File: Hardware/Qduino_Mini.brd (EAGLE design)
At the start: 20.3 x 38.1 mm, 41 parts, among them J1 LiPo, Q1 PFET, U1 ATMEGA32U41:1-LESS_PASTE, U2 MCP73831, U3 MAX17048, U4 AP2112K-3.3TRG-1, U5 MIGHTYQ-L-SILK, Y1 8MHZ

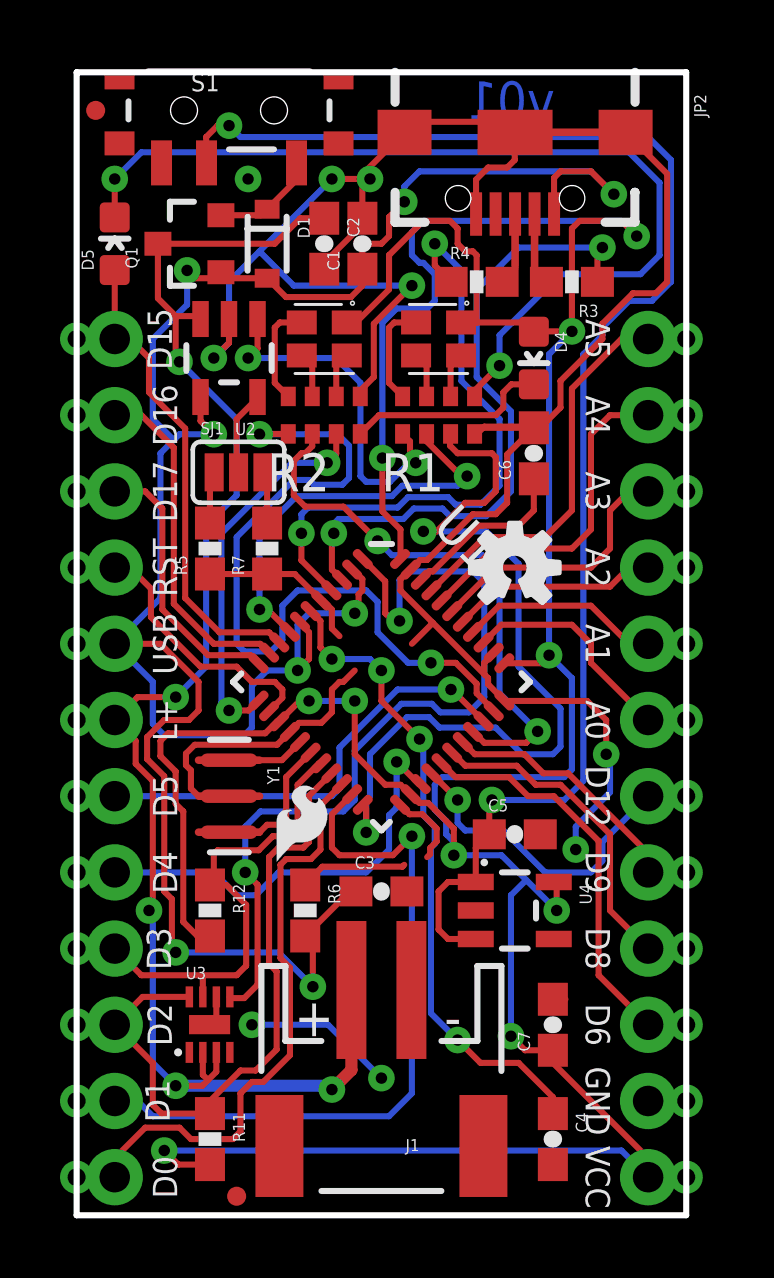
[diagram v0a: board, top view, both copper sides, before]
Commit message: Labled LED flags to the colors ther were hooked up to and replaced the RGB LEDs with the footprint for the new part.  STUFF IS BROKEN.
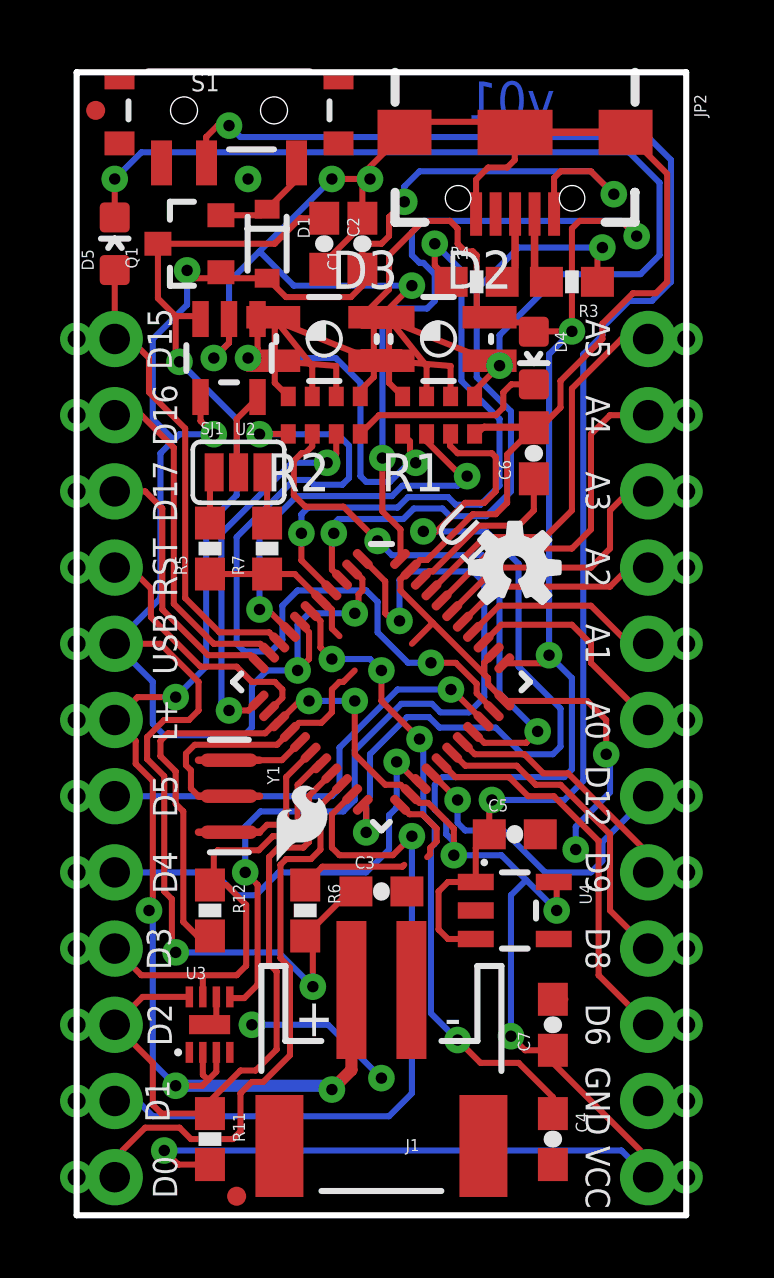
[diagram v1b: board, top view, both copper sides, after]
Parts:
- D2, D3: device Spark:PLCC4-2MM-RGB -> Testing:P-LCC-4-3
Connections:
- net N$1: now also D2.3; no longer D2.RED
- net N$2: now also D2.2; no longer D2.BLUE
- net N$32: now also D3.2; no longer D3.BLUE
- net N$34: now also D2.1; no longer D2.GREEN
- net N$35: now also D3.3; no longer D3.RED
- net N$37: now also D3.1; no longer D3.GREEN
- net VCC: now also D2.4, D3.4; no longer D2.CA, D3.CA
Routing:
- net N$35: track 3.45 -> 6.15 mm
- net N$1: track 3.45 -> 6.15 mm
- net N$2: track 1.51 -> 3.12 mm
- net N$32: track 1.51 -> 3.12 mm
- net N$37: track 1.51 -> 3.10 mm
- net N$34: track 1.51 -> 3.10 mm
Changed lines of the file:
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@@
 <element name="LOGO1" library="SparkFun-Aesthetics" package="OSHW-LOGO-S" value="OSHW-LOGOS" x="14.605" y="21.59"/>
 <element name="LOGO2" library="SparkFun-Aesthetics" package="SFE_LOGO_FLAME_.1" value="SFE_LOGO_FLAME.1_INCH" x="3.175" y="34.29" rot="MR0"/>
-<element name="D2" library="Spark" package="PLCC4-2MM-RGB" value="" x="12.065" y="29.21" rot="R90"/>
-<element name="D3" library="Spark" package="PLCC4-2MM-RGB" value="" x="8.255" y="29.21" rot="R90"/>
+<element name="D2" library="Testing" package="P-LCC-4-3" value="" x="12.065" y="29.21" rot="R90"/>
+<element name="D3" library="Testing" package="P-LCC-4-3" value="" x="8.255" y="29.21" rot="R90"/>
 <element name="R1" library="SparkFun-Passives" package="0603-ARV" value="330" x="12.065" y="26.67"/>
 <element name="R2" library="SparkFun-Passives" package="0603-ARV" value="330" x="8.255" y="26.67"/>
@@
 <contactref element="R11" pad="2"/>
 <contactref element="R12" pad="2"/>
-<contactref element="D2" pad="CA"/>
-<contactref element="D3" pad="CA"/>
+<contactref element="D2" pad="4"/>
+<contactref element="D3" pad="4"/>
 <contactref element="JP3" pad="1"/>
 <via x="20.32" y="1.27" extent="1-16" drill="0.6"/>
@@
 <wire x1="14.478" y1="5.969" x2="14.478" y2="10.668" width="0.2032" layer="16"/>
 <wire x1="14.478" y1="10.668" x2="14.986" y2="11.176" width="0.2032" layer="16"/>
-<wire x1="12.815" y1="29.76" x2="13.335" y2="29.76" width="0.2032" layer="1"/>
+<wire x1="13.765" y1="29.935" x2="13.335" y2="29.76" width="0.2032" layer="1"/>
 <wire x1="13.335" y1="29.76" x2="14.932" y2="29.76" width="0.2032" layer="1"/>
 <wire x1="14.932" y1="29.76" x2="15.24" y2="29.452" width="0.2032" layer="1"/>
 <wire x1="13.335" y1="32.004" x2="13.335" y2="29.76" width="0.2032" layer="1"/>
-<wire x1="9.005" y1="29.76" x2="9.313" y2="29.76" width="0.2032" layer="1"/>
+<wire x1="9.955" y1="29.935" x2="9.313" y2="29.76" width="0.2032" layer="1"/>
 <wire x1="9.313" y1="29.76" x2="10.414" y2="30.861" width="0.2032" layer="1"/>
 <wire x1="12.573" y1="12.0015" x2="12.573" y2="12.8905" width="0.2032" layer="1"/>
@@
 </signal>
 <signal name="N$34">
-<contactref element="D2" pad="GREEN"/>
+<contactref element="D2" pad="1"/>
 <contactref element="R1" pad="7"/>
 <wire x1="11.665" y1="27.295" x2="11.665" y2="28.31" width="0.2032" layer="1"/>
-<wire x1="11.665" y1="28.31" x2="11.315" y2="28.66" width="0.2032" layer="1"/>
+<wire x1="11.665" y1="28.31" x2="10.365" y2="29.935" width="0.2032" layer="1"/>
 </signal>
 <signal name="N$35">
-<contactref element="D3" pad="RED"/>
+<contactref element="D3" pad="3"/>
 <contactref element="R2" pad="8"/>
-<wire x1="7.505" y1="29.76" x2="6.773" y2="29.76" width="0.2032" layer="1"/>
+<wire x1="9.955" y1="28.485" x2="6.773" y2="29.76" width="0.2032" layer="1"/>
 <wire x1="6.773" y1="29.76" x2="6.604" y2="29.591" width="0.2032" layer="1"/>
 <wire x1="6.604" y1="29.591" x2="6.604" y2="27.746" width="0.2032" layer="1"/>
@@
 </signal>
 <signal name="N$37">
-<contactref element="D3" pad="GREEN"/>
+<contactref element="D3" pad="1"/>
 <contactref element="R2" pad="7"/>
 <wire x1="7.855" y1="27.295" x2="7.855" y2="28.31" width="0.2032" layer="1"/>
-<wire x1="7.855" y1="28.31" x2="7.505" y2="28.66" width="0.2032" layer="1"/>
+<wire x1="7.855" y1="28.31" x2="6.555" y2="29.935" width="0.2032" layer="1"/>
 </signal>
 <signal name="N$1">
-<contactref element="D2" pad="RED"/>
+<contactref element="D2" pad="3"/>
 <contactref element="R1" pad="8"/>
-<wire x1="11.315" y1="29.76" x2="10.583" y2="29.76" width="0.2032" layer="1"/>
+<wire x1="13.765" y1="28.485" x2="10.583" y2="29.76" width="0.2032" layer="1"/>
 <wire x1="10.583" y1="29.76" x2="10.414" y2="29.591" width="0.2032" layer="1"/>
 <wire x1="10.414" y1="29.591" x2="10.414" y2="27.746" width="0.2032" layer="1"/>
@@
 </signal>
 <signal name="N$32">
-<contactref element="D3" pad="BLUE"/>
+<contactref element="D3" pad="2"/>
 <contactref element="R2" pad="6"/>
 <wire x1="8.655" y1="27.295" x2="8.655" y2="28.31" width="0.2032" layer="1"/>
-<wire x1="8.655" y1="28.31" x2="9.005" y2="28.66" width="0.2032" layer="1"/>
+<wire x1="8.655" y1="28.31" x2="6.555" y2="28.485" width="0.2032" layer="1"/>
 </signal>
 <signal name="N$5">
@@
 <signal name="N$2">
 <contactref element="R1" pad="6"/>
-<contactref element="D2" pad="BLUE"/>
+<contactref element="D2" pad="2"/>
 <wire x1="12.465" y1="27.295" x2="12.465" y2="28.31" width="0.2032" layer="1"/>
-<wire x1="12.465" y1="28.31" x2="12.815" y2="28.66" width="0.2032" layer="1"/>
+<wire x1="12.465" y1="28.31" x2="10.365" y2="28.485" width="0.2032" layer="1"/>
 </signal>
 <signal name="N$4">

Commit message: Quin reworked the layout to fit the correct footprints for the LEDs he bought
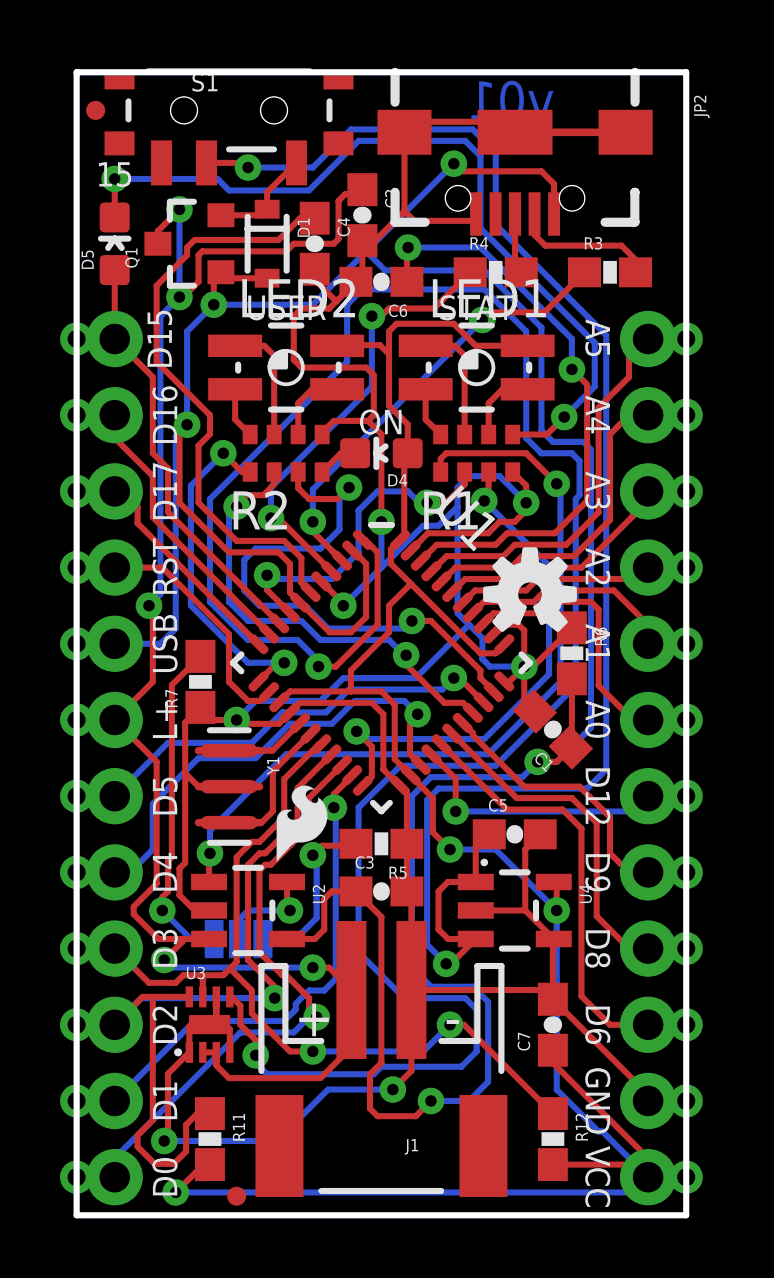
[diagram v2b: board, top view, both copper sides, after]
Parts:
- removed D2, D3: (no value), Testing:P-LCC-4-3
- added LED1, LED2: (no value), Testing:P-LCC-4-3
- moved C4 30.9 mm to (7.94, 32.4)
- moved U2 18.4 mm to (5.71, 10.2), turned to 270 degrees
- moved C1 17.4 mm to (15.9, 16.2), turned to 135 degrees
- moved SJ1 15.6 mm to (5.40, 9.21), flipped to the bottom
- moved R12 13.7 mm to (15.9, 2.54)
- moved R6 12.3 mm to (16.5, 18.7)
- moved R5 11.4 mm to (10.2, 12.4), turned to 180 degrees
- moved U5 10.2 mm to (10.2, 15.9)
- moved C6 7.65 mm to (10.2, 31.1), turned to 180 degrees
- moved D4 5.99 mm to (10.2, 25.4), turned to 90 degrees
- moved R7 4.97 mm to (4.13, 17.8)
- moved R1 1.80 mm to (13.3, 25.4)
- moved R2 1.80 mm to (6.99, 25.4)
- moved C2 1.59 mm to (9.53, 33.3)
- moved R3 1.31 mm to (17.8, 31.4), turned to 0 degrees
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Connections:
- removed net N$32: D3.2, R2.6
- removed net N$35: D3.3, R2.8
- new net N$3: LED2.3, R2.6
- new net N$8: LED2.2, R2.8
- net D11: now also R2.1; no longer R2.3
- net D13: now also R2.3; no longer R2.1
- net N$1: now also LED1.3, R1.6; no longer D2.3, R1.8
- net N$2: now also LED1.2, R1.8; no longer D2.2, R1.6
- net N$34: now also LED1.1; no longer D2.1
- net N$37: now also LED2.1; no longer D3.1
- net VCC: now also LED1.4, LED2.4; no longer D2.4, D3.4
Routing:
- net VCC: track 123.1 -> 77.7 mm, vias 11 -> 4
- net ALRT: track 28.5 -> 72.3 mm
- net GND: track 106.6 -> 138.1 mm, vias 10 -> 8
- net VBUS: track 80.2 -> 106.4 mm, vias 9 -> 6
- net STAT: track 12.0 -> 26.9 mm
- net AREF: track 5.78 -> 19.9 mm, vias 0 -> 2
- net SCL: track 17.2 -> 29.4 mm, vias 1 -> 3
- net RXLED: track 27.6 -> 17.3 mm
- net N$6: track 1.75 -> 11.1 mm, vias 0 -> 1
- net TX: track 25.4 -> 17.5 mm
- net D13: track 26.1 -> 18.8 mm
- net D-: track 21.8 -> 15.3 mm
- net N$35: track 6.15 -> 0.00 mm
- net D+: track 20.6 -> 14.8 mm
- net N$4: track 6.77 -> 1.36 mm
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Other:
- board text added: "15"
- board text added: "ON"
- board text added: "STAT"
- board text added: "USER"

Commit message: Added more ground pour, removed acid traps, cosmetic tweaks
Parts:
- D4: value PWR / GRN -> GREEN
- D5: value L / YLW -> Yellow
- renumbered LED1 to D2, LED2 to D3
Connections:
- net ALRT renamed !ALRT
- net RST renamed !RST
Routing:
- net GND: track 138.1 -> 130.2 mm, vias 8 -> 12
- net LIPO: track 55.3 -> 57.2 mm

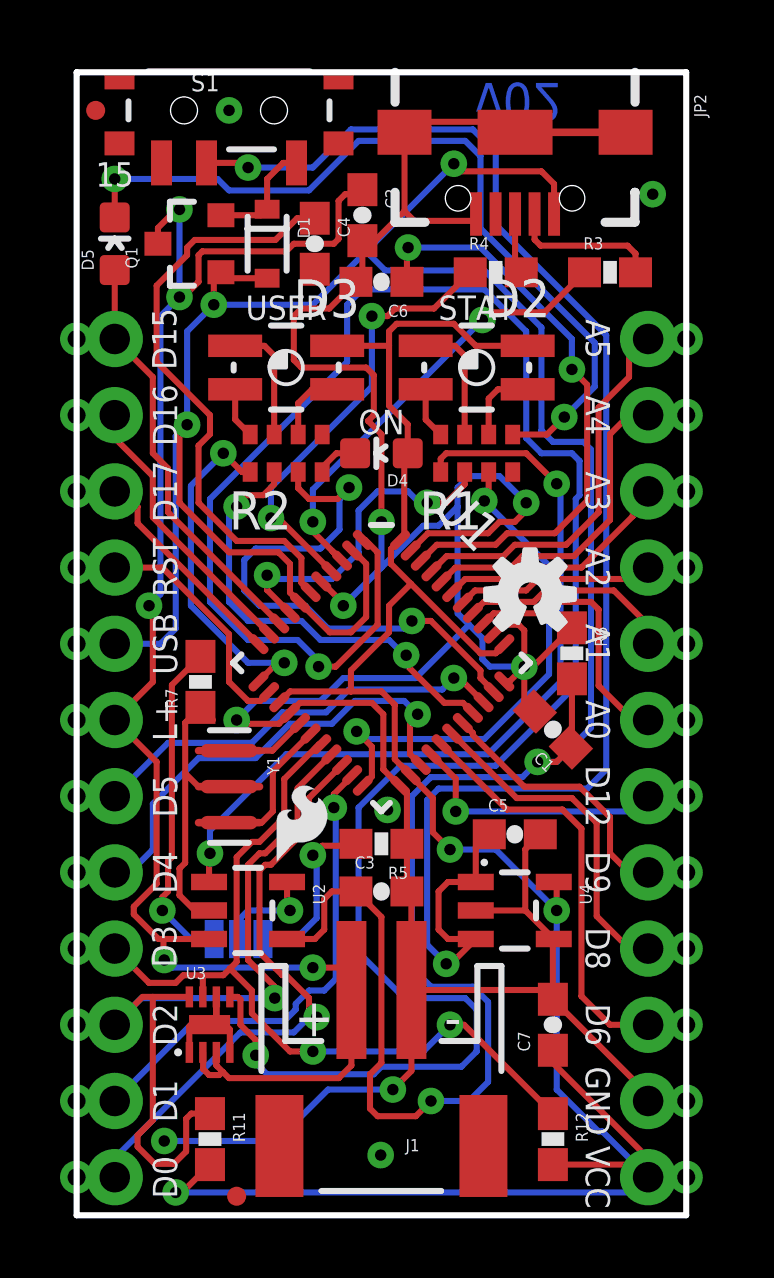
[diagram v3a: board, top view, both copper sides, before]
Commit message: Shifted things, added vias to pads & added more silk.
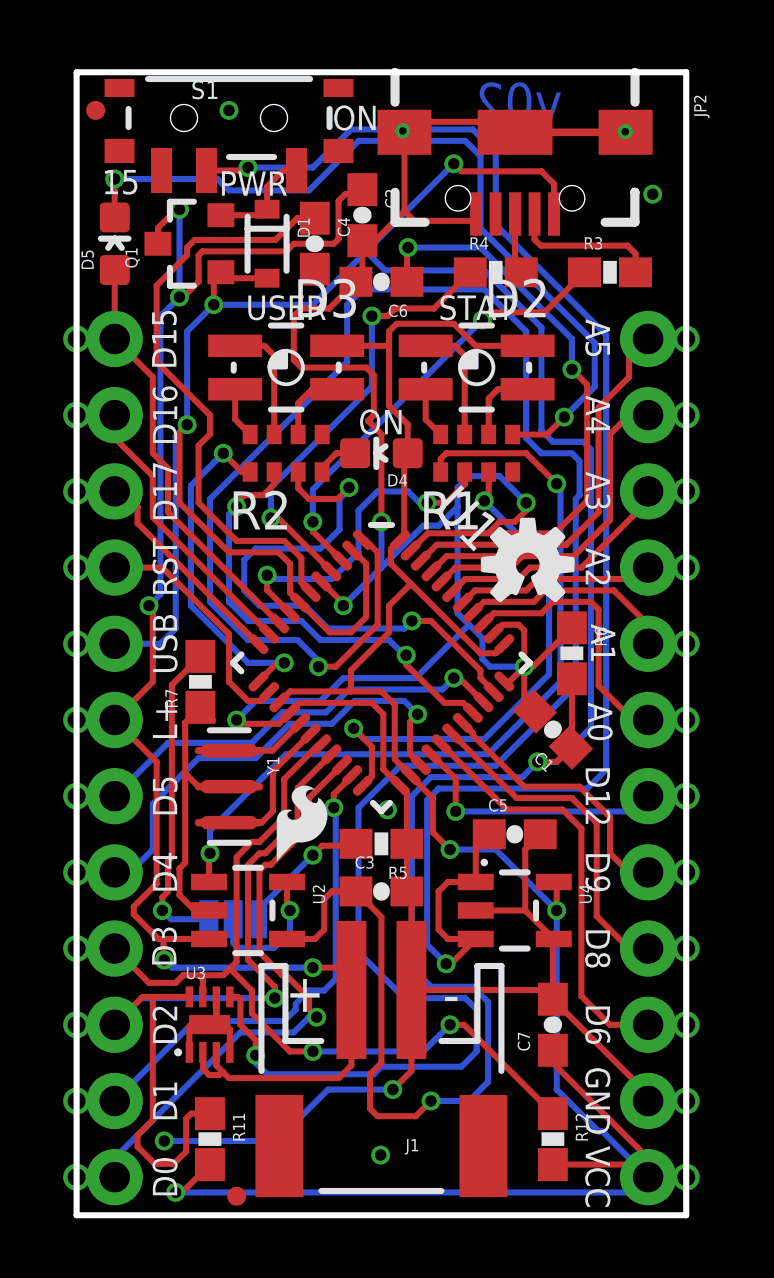
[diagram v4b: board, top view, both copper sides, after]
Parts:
- moved LOGO1 0.99 mm to (15.0, 21.7)
- moved SJ1 0.68 mm to (5.22, 9.87)
- moved S1 0.25 mm to (5.08, 36.6)
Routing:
- net N$7: track 5.84 -> 4.49 mm
- net PROG: track 3.47 -> 4.67 mm
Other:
- board text added: "PWR"
- board text added: "Qduino Mini"
- board text added: "SJ1"

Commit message: internally connected solder jumper, moved traces around new vias on USB
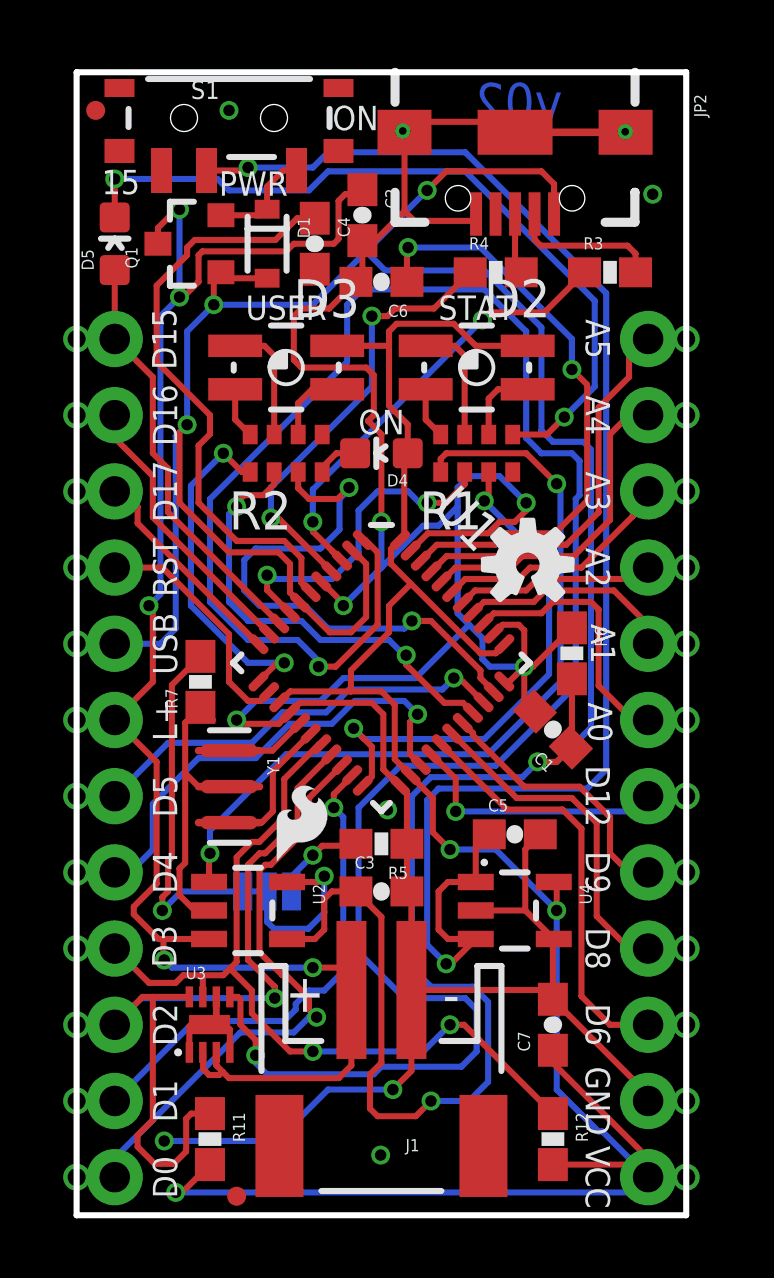
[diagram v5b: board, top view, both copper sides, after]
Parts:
- SJ1: device SparkFun-Passives:PAD-JUMPER-3-2OF3_NC_BY_PASTE_YES_SILK_FULL_BOX -> SparkFun-Passives:PAD-JUMPER-3-2OF3_NC_BY_TRACE_YES_SILK_FULL_BOX
- moved SJ1 1.46 mm to (6.35, 10.8)
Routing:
- net N$5: track 27.2 -> 25.7 mm
- net N$7: track 4.49 -> 3.09 mm
- net N$6: track 10.7 -> 11.9 mm
- net VINPUT: track 51.9 -> 50.6 mm
- net PROG: track 4.67 -> 5.78 mm
